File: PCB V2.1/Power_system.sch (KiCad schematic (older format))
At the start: 0 parts

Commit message: SunLeaf Alpha 0.2 and KiCAD Port
SunLeaf rev 2 called Alhpa 0.2 or 0.2a is the main component of this
commit. The entire hardware project has been ported to KiCAD libaries
and all. 0.2a features a revised formfactor, better ESP module, and many
fixes over the original. This version will also be capable of OTA
updates.
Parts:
- added C19, C20: CL05A105KA5NQNC, PCB_Footprints:C0402, symbol CL05A105KA5NQNC
- added C21: CL10A106KQ8NNNC, PCB_Footprints:C0603, symbol CL10A106KQ8NNNC
- added D1: BAT20JFILM, PCB_Footprints:BAT20JFILM, symbol BAT20JFILM
- added J3: S2B-PH-K-S(LF)(SN), PCB_Footprints:S2B-PH-K-S(LF)(SN), symbol S2B-PH-K-S(LF)(SN)
- added J4: S3B-PH-K-S(LF)(SN), PCB_Footprints:S3B-PH-K-S(LF)(SN), symbol S3B-PH-K-S(LF)(SN)
- added LED2: LTST-C191KGKT, PCB_Footprints:LED0603, symbol LTST-C191KGKT
- added LED3: LTST-C191KFKT, PCB_Footprints:LED0603, symbol LTST-C191KFKT
- added Q1, Q2: DMG2307L-7, PCB_Footprints:DMG2307L-7, symbol DMG2307L-7
- added R22: RC1005F4870CS, PCB_Footprints:R0402, symbol RC1005F4870CS
- added R23, R24, R25: RC2012F202CS, PCB_Footprints:R0805, symbol RC2012F202CS
- added U2: BQ24210DQCT, PCB_Footprints:BQ24210, symbol BQ24210DQCT
- added U3: AZ1117CR-3.3TRG1_1, PCB_Footprints:AZ1117CR-3.3TRG1, symbol AZ1117CR-3.3TRG1_1
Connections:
- net labels added: +3.3V, BAT, GND, THERM
- wire segments 0 -> 33
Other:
- note added: "Battery Charge Controller and Power Supply\n"

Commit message: Update
Updating KiCAD to the latest to get rounded corner pad support, filing
this commit as a backup of the project before update.
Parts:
- removed J3: S2B-PH-K-S(LF)(SN), PCB_Footprints:S2B-PH-K-S(LF)(SN), symbol S2B-PH-K-S(LF)(SN)
- removed J4: S3B-PH-K-S(LF)(SN), PCB_Footprints:S3B-PH-K-S(LF)(SN), symbol S3B-PH-K-S(LF)(SN)
- added J3: S2B-PH-SM4-TB(LF)(SN), PCB_Footprints:S2B-PH-SM4-TB(LF)(SN), symbol S2B-PH-SM4-TB(LF)(SN)
- added J4: S3B-PH-SM4-TB(LF)(SN), PCB_Footprints:S3B-PH-SM4-TB(LF)(SN), symbol S3B-PH-SM4-TB(LF)(SN)
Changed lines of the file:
@@
 Connection ~ 10325 2900
 $Comp
-L +3.3V #PWR029
+L +3.3V #PWR34
 U 1 1 57D80E79
 P 10875 2900
-F 0 "#PWR029" H 10875 2750 50  0001 C CNN
+F 0 "#PWR34" H 10875 2750 50  0001 C CNN
 F 1 "+3.3V" H 10875 3040 50  0000 C CNN
 F 2 "" H 10875 2900 50  0000 C CNN
@@
 $EndComp
 $Comp
-L GND #PWR030
+L GND #PWR33
 U 1 1 57D80F19
 P 9600 3350
-F 0 "#PWR030" H 9600 3100 50  0001 C CNN
+F 0 "#PWR33" H 9600 3100 50  0001 C CNN
 F 1 "GND" H 9600 3200 50  0000 C CNN
 F 2 "" H 9600 3350 50  0000 C CNN
@@
 Connection ~ 6000 3325
 $Comp
-L GND #PWR031
+L GND #PWR32
 U 1 1 57D82F5E
 P 5225 4600
-F 0 "#PWR031" H 5225 4350 50  0001 C CNN
+F 0 "#PWR32" H 5225 4350 50  0001 C CNN
 F 1 "GND" H 5225 4450 50  0000 C CNN
 F 2 "" H 5225 4600 50  0000 C CNN
@@
 $EndComp
 $Comp
-L GND #PWR032
+L GND #PWR31
 U 1 1 57D853F5
 P 4100 3350
-F 0 "#PWR032" H 4100 3100 50  0001 C CNN
+F 0 "#PWR31" H 4100 3100 50  0001 C CNN
 F 1 "GND" H 4100 3200 50  0000 C CNN
 F 2 "" H 4100 3350 50  0000 C CNN
@@
 $EndComp
 $Comp
-L S3B-PH-K-S(LF)(SN) J4
-U 1 1 57D893C2
-P 1725 4050
-F 0 "J4" H 1675 4225 60  0000 C CNN
-F 1 "S3B-PH-K-S(LF)(SN)" H 2125 3875 60  0000 C CNN
-F 2 "PCB_Footprints:S3B-PH-K-S(LF)(SN)" H 1575 4125 60  0001 C CNN
-F 3 "http://www.jst-mfg.com/product/pdf/eng/ePH.pdf" H 1450 4425 60  0001 C CNN
-F 4 "0.07217 @ 5000" H 1550 4525 60  0001 C CNN "Cost"
-F 5 "9 Sept 2016" H 1650 4625 60  0001 C CNN "Date Created "
-F 6 "9 Sept 2016" H 1750 4725 60  0001 C CNN "Date Modified"
-F 7 "Adam Vadala-Roth" H 1850 4825 60  0001 C CNN "Designer "
-F 8 "5.5mm" H 1950 4925 60  0001 C CNN "Height"
-F 9 "Yes" H 2050 5025 60  0001 C CNN "RHoS?"
-F 10 "JST Sales America Inc" H 2150 5125 60  0001 C CNN "MFR"
-F 11 "S3B-PH-K-S(LF)(SN)" H 2250 5225 60  0001 C CNN "MFR#"
-F 12 "Through Hole" H 2350 5325 60  0001 C CNN "Mounting"
-F 13 "3" H 2450 5425 60  0001 C CNN "Pin Count#"
-F 14 "Active" H 2550 5525 60  0001 C CNN "Status"
-F 15 "N/A" H 2650 5625 60  0001 C CNN "Tolerance"
-F 16 "Through Hole right angle connector." H 2750 5725 60  0001 C CNN "Type"
-F 17 "N/A" H 2850 5825 60  0001 C CNN "Voltage"
-F 18 "N/A" H 2950 5925 60  0001 C CNN "Wattage"
-F 19 "N/A" H 3050 6025 60  0001 C CNN "Component-Value"
-F 20 "3 Positions Header, Shrouded Connector 0.079\" (2.00mm) Through Hole, Right Angle Tin" H 3150 6125 60  0001 C CNN "Description"
-	1    1725 4050
-	1    0    0    -1
-$EndComp
-$Comp
-L S2B-PH-K-S(LF)(SN) J3
-U 1 1 57D89682
-P 1725 3625
-F 0 "J3" H 1675 3800 60  0000 C CNN
-F 1 "S2B-PH-K-S(LF)(SN)" H 2100 3525 60  0000 C CNN
-F 2 "PCB_Footprints:S2B-PH-K-S(LF)(SN)" H 1575 3700 60  0001 C CNN
-F 3 "http://www.jst-mfg.com/product/pdf/eng/ePH.pdf" H 1450 4000 60  0001 C CNN
-F 4 "0.06152 @ 5000" H 1550 4100 60  0001 C CNN "Cost"
-F 5 "9 Sept 2016" H 1650 4200 60  0001 C CNN "Date Created "
-F 6 "9 Sept 2016" H 1750 4300 60  0001 C CNN "Date Modified"
-F 7 "Adam Vadala-Roth" H 1850 4400 60  0001 C CNN "Designer "
-F 8 "5.5mm" H 1950 4500 60  0001 C CNN "Height"
-F 9 "Yes" H 2050 4600 60  0001 C CNN "RHoS?"
-F 10 "JST Sales America Inc" H 2150 4700 60  0001 C CNN "MFR"
-F 11 "S2B-PH-K-S(LF)(SN)" H 2250 4800 60  0001 C CNN "MFR#"
-F 12 "Through Hole" H 2350 4900 60  0001 C CNN "Mounting"
-F 13 "2" H 2450 5000 60  0001 C CNN "Pin Count#"
-F 14 "Active" H 2550 5100 60  0001 C CNN "Status"
-F 15 "N/A" H 2650 5200 60  0001 C CNN "Tolerance"
-F 16 "Through Hole right angle connector." H 2750 5300 60  0001 C CNN "Type"
-F 17 "N/A" H 2850 5400 60  0001 C CNN "Voltage"
-F 18 "N/A" H 2950 5500 60  0001 C CNN "Wattage"
-F 19 "N/A" H 3050 5600 60  0001 C CNN "Component-Value"
-F 20 "2 Positions Header, Shrouded Connector 0.079\" (2.00mm) Through Hole, Right Angle Tin" H 3150 5700 60  0001 C CNN "Description"
-	1    1725 3625
-	1    0    0    -1
-$EndComp
-$Comp
-L GND #PWR033
+L GND #PWR30
 U 1 1 57D89874
 P 2750 3625
-F 0 "#PWR033" H 2750 3375 50  0001 C CNN
+F 0 "#PWR30" H 2750 3375 50  0001 C CNN
 F 1 "GND" H 2750 3475 50  0000 C CNN
 F 2 "" H 2750 3625 50  0000 C CNN
@@
 Connection ~ 2200 2900
 $Comp
-L GND #PWR034
+L GND #PWR29
 U 1 1 57D8ABE6
 P 2725 4125
-F 0 "#PWR034" H 2725 3875 50  0001 C CNN
+F 0 "#PWR29" H 2725 3875 50  0001 C CNN
 F 1 "GND" H 2725 3975 50  0000 C CNN
 F 2 "" H 2725 4125 50  0000 C CNN
@@
 Text Notes 2375 1675 0    197  ~ 39
 Battery Charge Controller and Power Supply\n
+$Comp
+L S3B-PH-SM4-TB(LF)(SN) J4
+U 1 1 57DB73BE
+P 1725 4050
+F 0 "J4" H 1675 4225 60  0000 C CNN
+F 1 "S3B-PH-SM4-TB(LF)(SN)" H 2125 3875 60  0000 C CNN
+F 2 "PCB_Footprints:S3B-PH-SM4-TB(LF)(SN)" H 1575 4125 60  0001 C CNN
+F 3 "http://www.jst-mfg.com/product/pdf/eng/ePH.pdf" H 1450 4425 60  0001 C CNN
+F 4 "0.28250 @ 5000" H 1550 4525 60  0001 C CNN "Cost"
+F 5 "9 Sept 2016" H 1650 4625 60  0001 C CNN "Date Created "
+F 6 "9 Sept 2016" H 1750 4725 60  0001 C CNN "Date Modified"
+F 7 "Adam Vadala-Roth" H 1850 4825 60  0001 C CNN "Designer "
+F 8 "5.5mm" H 1950 4925 60  0001 C CNN "Height"
+F 9 "Yes" H 2050 5025 60  0001 C CNN "RHoS?"
+F 10 "JST Sales America Inc" H 2150 5125 60  0001 C CNN "MFR"
+F 11 "S3B-PH-K-S(LF)(SN)" H 2250 5225 60  0001 C CNN "MFR#"
+F 12 "Through Hole" H 2350 5325 60  0001 C CNN "SMT/SMD"
+F 13 "3" H 2450 5425 60  0001 C CNN "Pin Count#"
+F 14 "Active" H 2550 5525 60  0001 C CNN "Status"
+F 15 "N/A" H 2650 5625 60  0001 C CNN "Tolerance"
+F 16 "Surface Mount Right Angle 3 Pin Connector" H 2750 5725 60  0001 C CNN "Type"
+F 17 "N/A" H 2850 5825 60  0001 C CNN "Voltage"
+F 18 "N/A" H 2950 5925 60  0001 C CNN "Wattage"
+F 19 "N/A" H 3050 6025 60  0001 C CNN "Component-Value"
+F 20 "3 Positions Header, Shrouded Connector 0.079\" (2.00mm) Surface Mount, Right Angle Tin" H 3150 6125 60  0001 C CNN "Description"
+	1    1725 4050
+	1    0    0    -1
+$EndComp
+$Comp
+L S2B-PH-SM4-TB(LF)(SN) J3
+U 1 1 57DB74B4
+P 1725 3625
+F 0 "J3" H 1675 3800 60  0000 C CNN
+F 1 "S2B-PH-SM4-TB(LF)(SN)" H 2100 3525 60  0000 C CNN
+F 2 "PCB_Footprints:S2B-PH-SM4-TB(LF)(SN)" H 1575 3700 60  0001 C CNN
+F 3 "http://www.jst-mfg.com/product/pdf/eng/ePH.pdf" H 1450 4000 60  0001 C CNN
+F 4 "0.24037 @ 5000" H 1550 4100 60  0001 C CNN "Cost"
+F 5 "9 Sept 2016" H 1650 4200 60  0001 C CNN "Date Created "
+F 6 "9 Sept 2016" H 1750 4300 60  0001 C CNN "Date Modified"
+F 7 "Adam Vadala-Roth" H 1850 4400 60  0001 C CNN "Designer "
+F 8 "5.5mm" H 1950 4500 60  0001 C CNN "Height"
+F 9 "Yes" H 2050 4600 60  0001 C CNN "RHoS?"
+F 10 "JST Sales America Inc" H 2150 4700 60  0001 C CNN "MFR"
+F 11 "S2B-PH-SM4-TB(LF)(SN)" H 2250 4800 60  0001 C CNN "MFR#"
+F 12 "SMT/SMD" H 2350 4900 60  0001 C CNN "Mounting"
+F 13 "2" H 2450 5000 60  0001 C CNN "Pin Count#"
+F 14 "Active" H 2550 5100 60  0001 C CNN "Status"
+F 15 "N/A" H 2650 5200 60  0001 C CNN "Tolerance"
+F 16 "Surface mount right angle 2 pin connector" H 2750 5300 60  0001 C CNN "Type"
+F 17 "N/A" H 2850 5400 60  0001 C CNN "Voltage"
+F 18 "N/A" H 2950 5500 60  0001 C CNN "Wattage"
+F 19 "N/A" H 3050 5600 60  0001 C CNN "Component-Value"
+F 20 "2 Positions Header, Shrouded Connector 0.079\" (2.00mm) Surface Mount, Right Angle Tin" H 3150 5700 60  0001 C CNN "Description"
+	1    1725 3625
+	1    0    0    -1
+$EndComp
 $EndSCHEMATC

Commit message: Placement
Heavy progress on component placement in KiCAD for SunLEaf V2,
committing to save progress, nightly builds of KiCAD are very crash
prone.
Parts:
- removed J3: S2B-PH-SM4-TB(LF)(SN), PCB_Footprints:S2B-PH-SM4-TB(LF)(SN), symbol S2B-PH-SM4-TB(LF)(SN)
- removed J4: S3B-PH-SM4-TB(LF)(SN), PCB_Footprints:S3B-PH-SM4-TB(LF)(SN), symbol S3B-PH-SM4-TB(LF)(SN)
- removed R23, R24, R25: RC2012F202CS, PCB_Footprints:R0805, symbol RC2012F202CS
- added J3: B2B-PH-K-S(LF)(SN), PCB_Footprints:B2B-PH-K-S(LF)(SN), symbol B2B-PH-K-S(LF)(SN)
- added J4: B3B-PH-K-S(LF)(SN), PCB_Footprints:B3B-PH-K-S(LF)(SN), symbol B3B-PH-K-S(LF)(SN)
- added R23: RC1005F102CS, PCB_Footprints:R0402, symbol RC1005F102CS
- added R24, R25: RC1608J202CS, PCB_Footprints:R0603, symbol RC1608J202CS

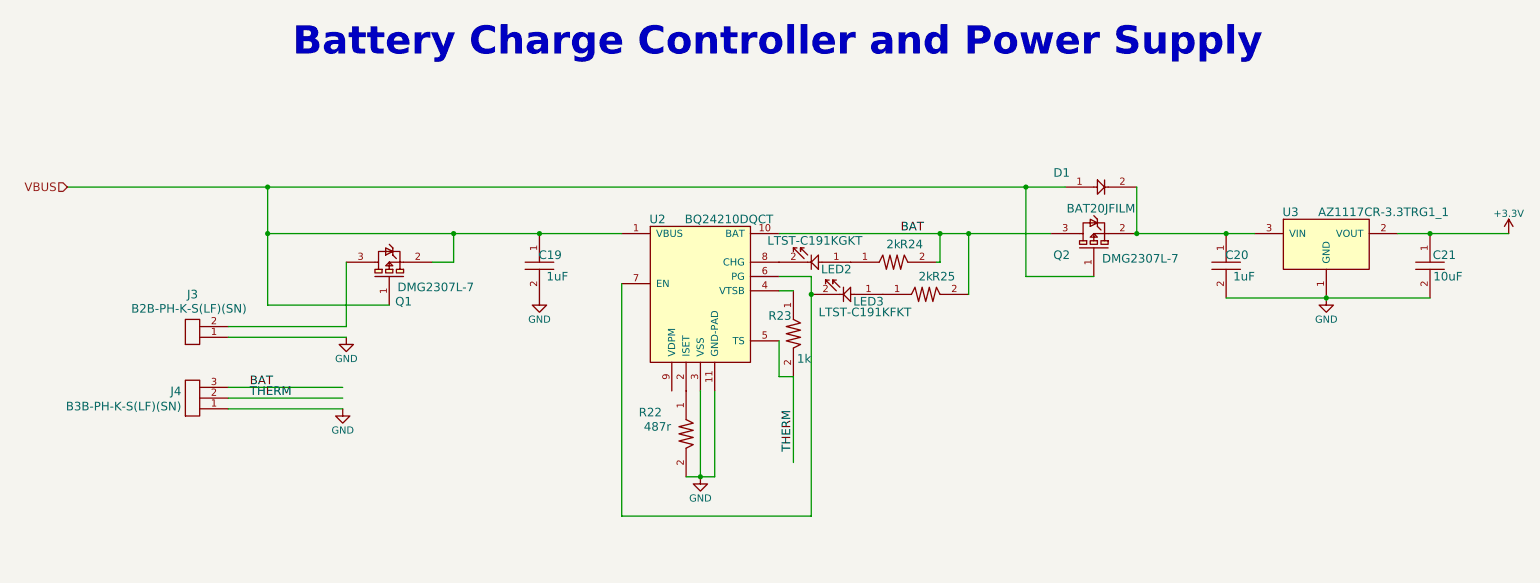
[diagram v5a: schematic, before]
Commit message: Battery Monitoring & OTA
OTA signals between both processors solidified and routed. Battery
monitoring added as voltage divider into ADC channel. All but done
pending some small tweaks.
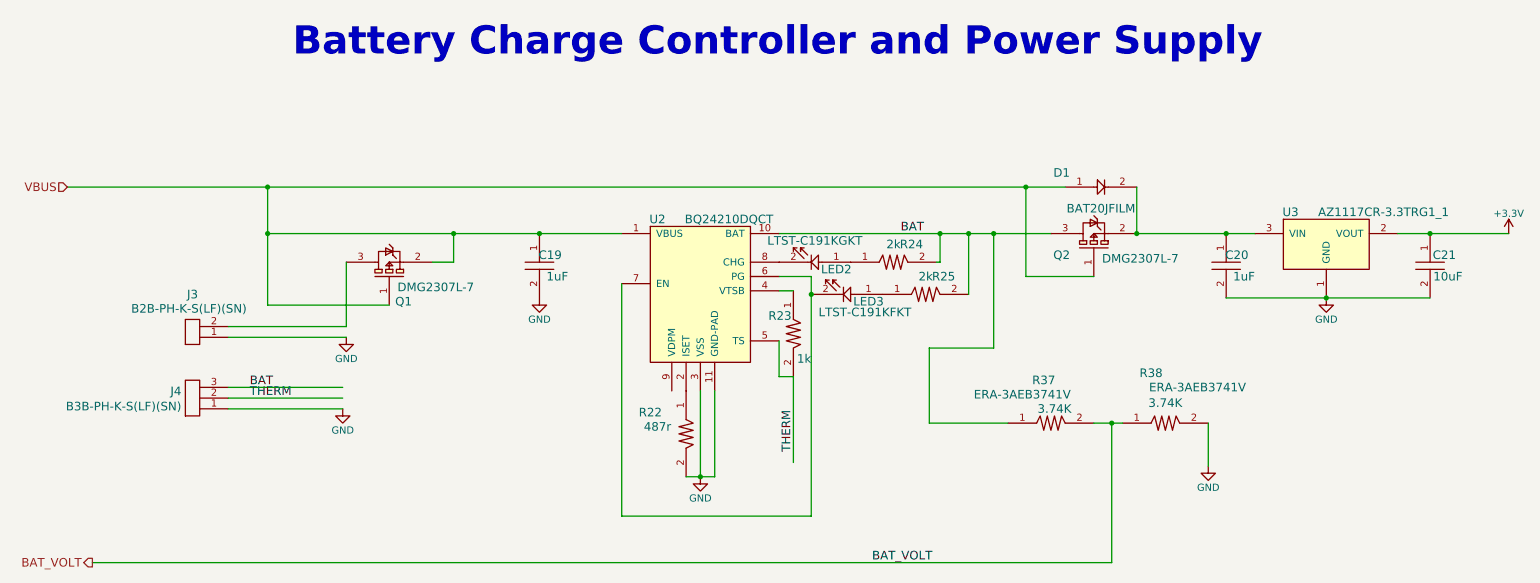
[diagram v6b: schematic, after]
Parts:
- added R37, R38: ERA-3AEB3741V, PCB_Footprints:R0603, symbol ERA-3AEB3741V
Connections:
- net labels added: BAT_VOLT
- wire segments 33 -> 55
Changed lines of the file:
@@
 $EndComp
 Wire Wire Line
-	800  2575 7775 2575
-Wire Wire Line
-	2200 2575 2200 3400
-Wire Wire Line
-	2200 2900 4675 2900
-Wire Wire Line
-	5775 2900 7675 2900
+	800  2575 2200 2575
+Wire Wire Line
+	2200 2575 7500 2575
+Wire Wire Line
+	7500 2575 7775 2575
+Wire Wire Line
+	2200 2575 2200 2900
+Wire Wire Line
+	2200 2900 2200 3400
+Wire Wire Line
+	2200 2900 3500 2900
+Wire Wire Line
+	3500 2900 4100 2900
+Wire Wire Line
+	4100 2900 4675 2900
+Wire Wire Line
+	5775 2900 6900 2900
+Wire Wire Line
+	6900 2900 7100 2900
+Wire Wire Line
+	7100 2900 7275 2900
+Wire Wire Line
+	7275 2900 7675 2900
 Wire Wire Line
 	8275 2575 8275 2900
@@
 Connection ~ 7500 2575
 Wire Wire Line
-	8275 2900 9100 2900
-Wire Wire Line
-	10100 2900 10875 2900
+	8275 2900 8900 2900
+Wire Wire Line
+	8900 2900 9100 2900
+Wire Wire Line
+	10100 2900 10325 2900
+Wire Wire Line
+	10325 2900 10875 2900
 Connection ~ 10325 2900
 $Comp
-L +3.3V #PWR031
+L +3.3V #PWR38
 U 1 1 57D80E79
 P 10875 2900
-F 0 "#PWR031" H 10875 2750 50  0001 C CNN
+F 0 "#PWR38" H 10875 2750 50  0001 C CNN
 F 1 "+3.3V" H 10875 3040 50  0000 C CNN
 F 2 "" H 10875 2900 50  0000 C CNN
@@
 $EndComp
 $Comp
-L GND #PWR032
+L GND #PWR37
 U 1 1 57D80F19
 P 9600 3350
-F 0 "#PWR032" H 9600 3100 50  0001 C CNN
+F 0 "#PWR37" H 9600 3100 50  0001 C CNN
 F 1 "GND" H 9600 3200 50  0000 C CNN
 F 2 "" H 9600 3350 50  0000 C CNN
@@
 $EndComp
 Wire Wire Line
-	8900 3350 10325 3350
+	8900 3350 9600 3350
+Wire Wire Line
+	9600 3350 10325 3350
 Connection ~ 9600 3350
 Connection ~ 8900 2900
@@
 	5775 3200 6000 3200
 Wire Wire Line
-	6000 3200 6000 4875
+	6000 3200 6000 3325
+Wire Wire Line
+	6000 3325 6000 4875
 Wire Wire Line
 	6000 4875 4675 4875
@@
 Connection ~ 6000 3325
 $Comp
-L GND #PWR033
+L GND #PWR35
 U 1 1 57D82F5E
 P 5225 4600
-F 0 "#PWR033" H 5225 4350 50  0001 C CNN
+F 0 "#PWR35" H 5225 4350 50  0001 C CNN
 F 1 "GND" H 5225 4450 50  0000 C CNN
 F 2 "" H 5225 4600 50  0000 C CNN
@@
 	5225 4000 5225 4600
 Wire Wire Line
-	5125 4600 5325 4600
+	5125 4600 5225 4600
+Wire Wire Line
+	5225 4600 5325 4600
 Wire Wire Line
 	5325 4600 5325 4000
@@
 $EndComp
 $Comp
-L GND #PWR034
+L GND #PWR34
 U 1 1 57D853F5
 P 4100 3350
-F 0 "#PWR034" H 4100 3100 50  0001 C CNN
+F 0 "#PWR34" H 4100 3100 50  0001 C CNN
 F 1 "GND" H 4100 3200 50  0000 C CNN
 F 2 "" H 4100 3350 50  0000 C CNN
@@
 $EndComp
 $Comp
-L GND #PWR035
+L GND #PWR33
 U 1 1 57D89874
 P 2750 3625
-F 0 "#PWR035" H 2750 3375 50  0001 C CNN
+F 0 "#PWR33" H 2750 3375 50  0001 C CNN
 F 1 "GND" H 2750 3475 50  0000 C CNN
 F 2 "" H 2750 3625 50  0000 C CNN
@@
 Connection ~ 2200 2900
 $Comp
-L GND #PWR036
+L GND #PWR32
 U 1 1 57D8ABE6
 P 2725 4125
-F 0 "#PWR036" H 2725 3875 50  0001 C CNN
+F 0 "#PWR32" H 2725 3875 50  0001 C CNN
 F 1 "GND" H 2725 3975 50  0000 C CNN
 F 2 "" H 2725 4125 50  0000 C CNN
@@
 $EndComp
 Connection ~ 4100 2900
+$Comp
+L ERA-3AEB3741V R37
+U 1 1 57E04D9F
+P 7675 4225
+F 0 "R37" H 7625 4525 60  0000 C CNN
+F 1 "ERA-3AEB3741V" H 7475 4425 60  0000 C CNN
+F 2 "PCB_Footprints:R0603" H 7275 4475 60  0001 C CNN
+F 3 "https://media.digikey.com/pdf/Data%20Sheets/Panasonic%20Electronic%20Components/ERA%201A,2A,3A,6A,8A.pdf" H 7375 4675 60  0001 C CNN
+F 4 "0.04275 @ 5000" H 9225 6175 60  0001 C CNN "Cost"
+F 5 "19 Sept 2016" H 7575 4775 60  0001 C CNN "Date Created"
+F 6 "19 Sept 2016" H 7675 4875 60  0001 C CNN "Date Modified"
+F 7 "Adam Vadala-Roth" H 7775 4975 60  0001 C CNN "Designer"
+F 8 "0.55mm" H 7875 5075 60  0001 C CNN "Height"
+F 9 "Yes" H 7975 5175 60  0001 C CNN "RHoS?"
+F 10 "Panasonic Electronic Components" H 8075 5275 60  0001 C CNN "MFR"
+F 11 "ERA-3AEB3741V" H 8175 5375 60  0001 C CNN "MFR#"
+F 12 "SMT/SMD" H 8275 5475 60  0001 C CNN "Mounting"
+F 13 "2" H 8375 5575 60  0001 C CNN "Pin Count#"
+F 14 "Active" H 8475 5675 60  0001 C CNN "Status"
+F 15 "1%" H 8575 5775 60  0001 C CNN "Tolerance"
+F 16 "passive" H 8675 5875 60  0001 C CNN "Type"
+F 17 "N/A" H 8775 5975 60  0001 C CNN "Voltage"
+F 18 "1/10" H 8875 6075 60  0001 C CNN "Wattage"
+F 19 "3.74K" H 7700 4325 60  0000 C CNN "Component-Value"
+F 20 "RES SMD 3.74KOHM 0.1% 1/10W 0603" H 9075 6275 60  0001 C CNN "Description"
+	1    7675 4225
+	1    0    0    -1
+$EndComp
+$Comp
+L ERA-3AEB3741V R38
+U 1 1 57E04FB0
+P 8475 4225
+F 0 "R38" H 8375 4575 60  0000 C CNN
+F 1 "ERA-3AEB3741V" H 8700 4475 60  0000 C CNN
+F 2 "PCB_Footprints:R0603" H 8075 4475 60  0001 C CNN
+F 3 "https://media.digikey.com/pdf/Data%20Sheets/Panasonic%20Electronic%20Components/ERA%201A,2A,3A,6A,8A.pdf" H 8175 4675 60  0001 C CNN
+F 4 "0.04275 @ 5000" H 10025 6175 60  0001 C CNN "Cost"
+F 5 "19 Sept 2016" H 8375 4775 60  0001 C CNN "Date Created"
+F 6 "19 Sept 2016" H 8475 4875 60  0001 C CNN "Date Modified"
+F 7 "Adam Vadala-Roth" H 8575 4975 60  0001 C CNN "Designer"
+F 8 "0.55mm" H 8675 5075 60  0001 C CNN "Height"
+F 9 "Yes" H 8775 5175 60  0001 C CNN "RHoS?"
+F 10 "Panasonic Electronic Components" H 8875 5275 60  0001 C CNN "MFR"
+F 11 "ERA-3AEB3741V" H 8975 5375 60  0001 C CNN "MFR#"
+F 12 "SMT/SMD" H 9075 5475 60  0001 C CNN "Mounting"
+F 13 "2" H 9175 5575 60  0001 C CNN "Pin Count#"
+F 14 "Active" H 9275 5675 60  0001 C CNN "Status"
+F 15 "1%" H 9375 5775 60  0001 C CNN "Tolerance"
+F 16 "passive" H 9475 5875 60  0001 C CNN "Type"
+F 17 "N/A" H 9575 5975 60  0001 C CNN "Voltage"
+F 18 "1/10" H 9675 6075 60  0001 C CNN "Wattage"
+F 19 "3.74K" H 8475 4366 60  0000 C CNN "Component-Value"
+F 20 "RES SMD 3.74KOHM 0.1% 1/10W 0603" H 9875 6275 60  0001 C CNN "Description"
+	1    8475 4225
+	1    0    0    -1
+$EndComp
+$Comp
+L GND #PWR36
+U 1 1 57E05471
+P 8775 4525
+F 0 "#PWR36" H 8775 4275 50  0001 C CNN
+F 1 "GND" H 8775 4375 50  0000 C CNN
+F 2 "" H 8775 4525 50  0000 C CNN
+F 3 "" H 8775 4525 50  0000 C CNN
+	1    8775 4525
+	1    0    0    -1
+$EndComp
+Wire Wire Line
+	8775 4225 8775 4525
+Wire Wire Line
+	8175 4225 8100 4225
+Wire Wire Line
+	8100 4225 7975 4225
+Wire Wire Line
+	8100 4225 8100 5200
+Wire Wire Line
+	8100 5200 975  5200
+Connection ~ 8100 4225
+Wire Wire Line
+	7375 4225 6825 4225
+Wire Wire Line
+	6825 4225 6825 3700
+Wire Wire Line
+	6825 3700 7275 3700
+Wire Wire Line
+	7275 3700 7275 2900
+Connection ~ 7275 2900
+Text Label 6425 5200 0    60   ~ 0
+BAT_VOLT
+Text HLabel 975  5200 0    60   Output ~ 0
+BAT_VOLT
 $EndSCHEMATC
